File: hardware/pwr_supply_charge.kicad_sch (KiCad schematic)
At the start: 26 parts, among them J1 Battery Input, J2 Power Switch, J3 USB_C_Receptacle_USB2.0_14P, Q1 PSMN1R5-30YL, Q2 PSMN1R5-30YL, Q3 AO4435, Q4 AO4468, U1 HY2120, U2 CN3302

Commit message: updating component placcement
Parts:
- C1, C2: footprint Capacitor_SMD:C_0201_0603Metric -> Capacitor_SMD:C_0402_1005Metric
- R1, R2, R3: footprint Resistor_SMD:R_0603_1608Metric -> Resistor_SMD:R_0402_1005Metric
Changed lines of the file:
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@@
 			)
 		)
-		(property "Footprint" "Resistor_SMD:R_0603_1608Metric"
+		(property "Footprint" "Resistor_SMD:R_0402_1005Metric"
 			(at 168.91 33.528 90)
 			(effects
@@
 			)
 		)
-		(property "Footprint" "Resistor_SMD:R_0603_1608Metric"
+		(property "Footprint" "Resistor_SMD:R_0402_1005Metric"
 			(at 161.29 39.878 90)
 			(effects
@@
 			)
 		)
-		(property "Footprint" "Resistor_SMD:R_0603_1608Metric"
+		(property "Footprint" "Resistor_SMD:R_0402_1005Metric"
 			(at 214.122 50.8 90)
 			(effects
@@
 			)
 		)
-		(property "Footprint" "Capacitor_SMD:C_0201_0603Metric"
+		(property "Footprint" "Capacitor_SMD:C_0402_1005Metric"
 			(at 177.4952 44.45 0)
 			(effects
@@
 			)
 		)
-		(property "Footprint" "Capacitor_SMD:C_0201_0603Metric"
+		(property "Footprint" "Capacitor_SMD:C_0402_1005Metric"
 			(at 167.3352 46.99 0)
 			(effects

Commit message: Updating component placement
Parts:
- C3, C4: footprint Capacitor_SMD:C_0805_2012Metric -> Capacitor_SMD:CP_Elec_4x4.5
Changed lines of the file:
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@@
 			)
 		)
-		(property "Footprint" "Capacitor_SMD:C_0805_2012Metric"
+		(property "Footprint" "Capacitor_SMD:CP_Elec_4x4.5"
 			(at 228.2952 113.03 0)
 			(effects
@@
 			)
 		)
-		(property "Footprint" "Capacitor_SMD:C_0805_2012Metric"
+		(property "Footprint" "Capacitor_SMD:CP_Elec_4x4.5"
 			(at 117.8052 107.95 0)
 			(effects

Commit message: adding 3d models
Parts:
- J1: footprint Connector_JST:JST_XH_B3B-XH-AM_1x03_P2.50mm_Vertical -> Connector_JST:JST_XH_B3B-XH-A_1x03_P2.50mm_Vertical
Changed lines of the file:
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@@
 			)
 		)
-		(property "Footprint" "Connector_JST:JST_XH_B3B-XH-AM_1x03_P2.50mm_Vertical"
+		(property "Footprint" "Connector_JST:JST_XH_B3B-XH-A_1x03_P2.50mm_Vertical"
 			(at 93.98 38.1 0)
 			(effects

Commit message: adding inductor 3d model
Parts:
- L1: footprint Inductor_SMD:L_7.3x7.3_H3.5 -> Chromapi_FP:INDM6864X300N
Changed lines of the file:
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@@
 			)
 		)
-		(property "Footprint" "Inductor_SMD:L_7.3x7.3_H3.5"
+		(property "Footprint" "Chromapi_FP:INDM6864X300N"
 			(at 204.47 97.79 0)
 			(effects

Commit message: Updating schematic
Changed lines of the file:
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@@
 					(size 1.27 1.27)
 				)
+				(hide yes)
 			)
 		)
@@
 					(size 1.27 1.27)
 				)
+				(hide yes)
 			)
 		)
@@
 					(size 1.27 1.27)
 				)
+				(hide yes)
 			)
 		)
@@
 					(size 1.27 1.27)
 				)
+				(hide yes)
 			)
 		)
@@
 					(size 1.27 1.27)
 				)
-			)
-		)
+				(hide yes)
+			)
+		)

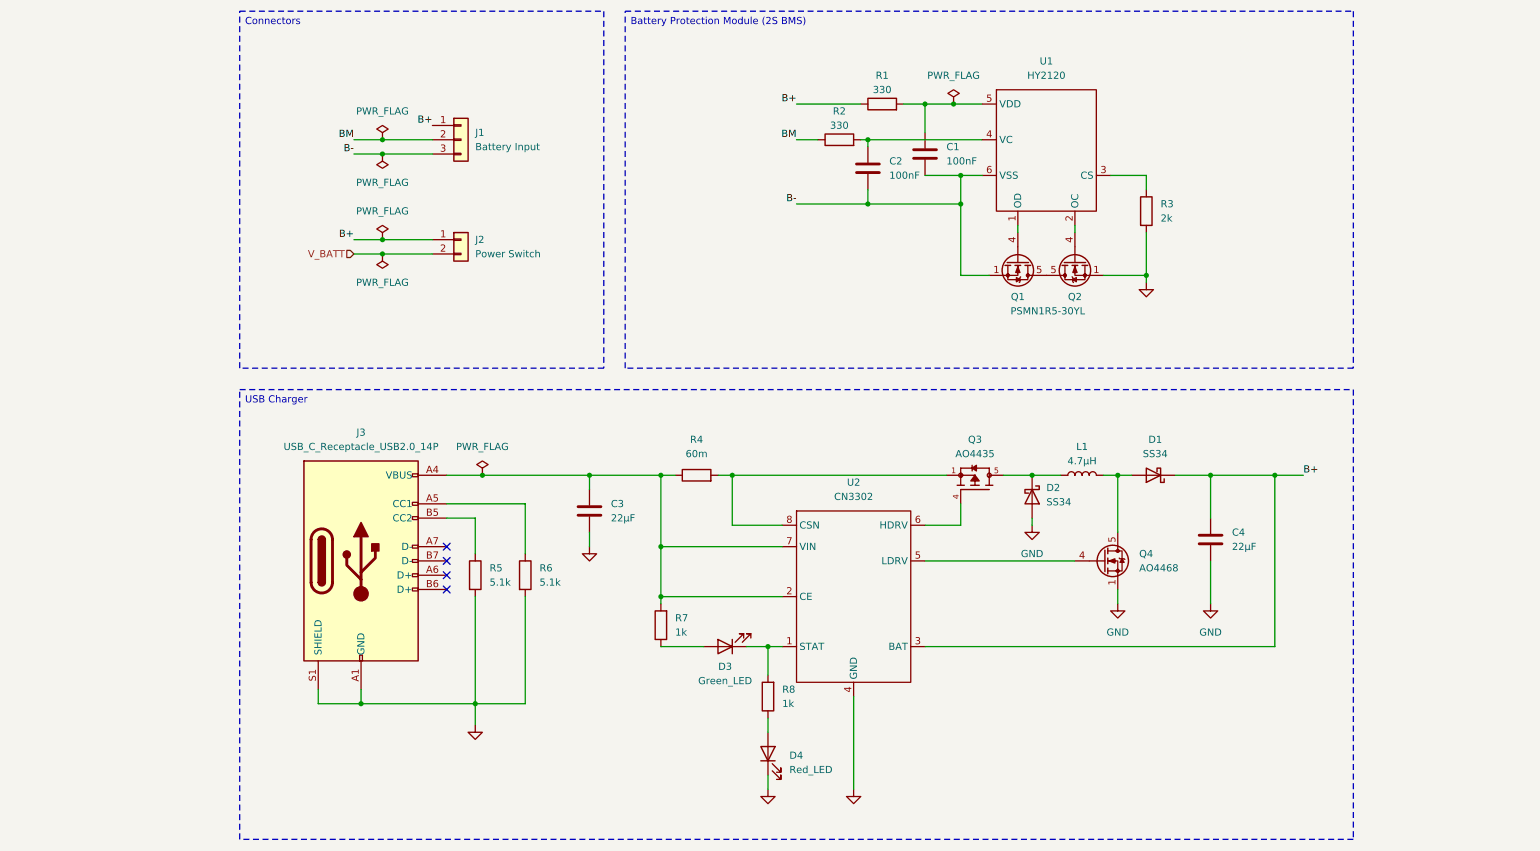
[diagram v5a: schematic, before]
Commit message: IMU modification and Power monitor addition
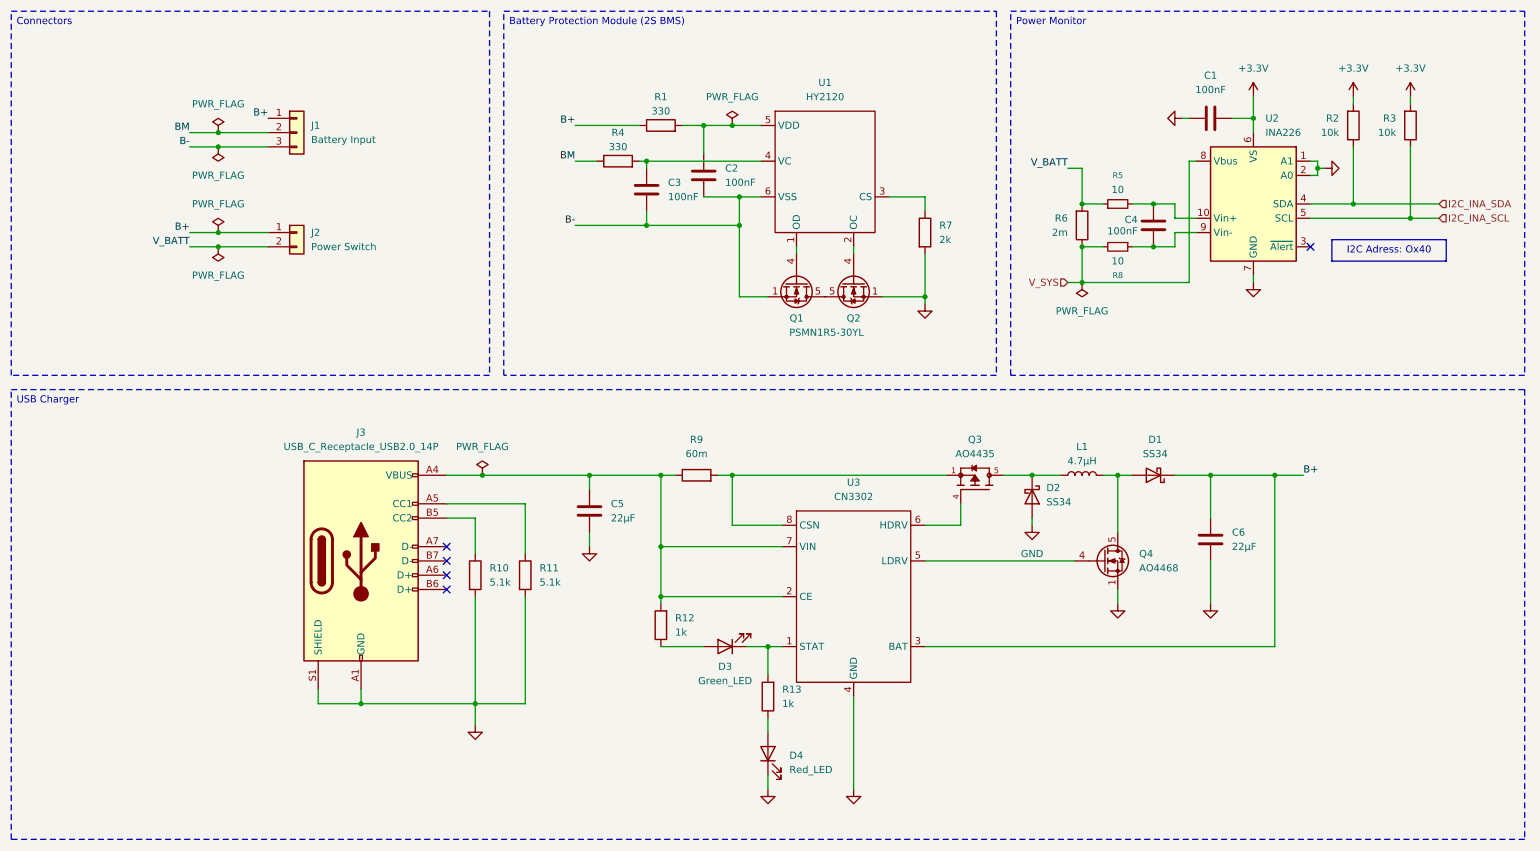
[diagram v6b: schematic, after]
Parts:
- added C1: 100nF, Capacitor_SMD:C_0603_1608Metric, symbol Device:C
- added C4: 100nF, Capacitor_SMD:CP_Elec_4x4.5, symbol Device:C
- added R2, R3: 10k, symbol Device:R
- added R5, R8: 10, symbol Device:R_Small
- added R6: 2m, symbol Device:R
- added U2: INA226, Package_SO:VSSOP-10_3x3mm_P0.5mm, symbol Sensor_Energy:INA226
- Q3: Availability In Stock -> (none); Description_1 P-Channel 30 V 10.5A (Ta) 3.1W (Ta) Surface Mount 8-SOIC -> (none); MANUFACTURER ALPHA & OMEGA SEMICONDUCTOR -> (none); MF Alpha & -> (none); MFN (none) -> Alpha & Omega Semiconductor; MP AO4435 -> (none); MPN (none) -> AO4435; Package SOIC-8 Alpha &amp; Omega Semiconductor -> SOIC-8 Alpha & Omega Semiconductor; Price None -> (none); SnapEDA_Link https://www.snapeda.com/parts/AO4435/Alpha/view-part/?ref=s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 -> (none)
- renumbered C1 to C2, C2 to C3, C3 to C5, C4 to C6, R5 to R10, R6 to R11, R7 to R12, R8 to R13, R2 to R4, R3 to R7, R4 to R9, U2 to U3
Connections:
- net GND: now also C1.2, U2.1 (A1), U2.2 (A0), U2.7 (GND)
- net V_BATT: now also R5.1, R6.2
- new net: C4.2, R8.1, U2.9 (Vin-)
- new net: C4.1, R5.2, U2.10 (Vin+)
- new net +3.3V: C1.1, R2.2, R3.2, U2.6 (VS)
- new net I2C_INA_SCL: R3.1, U2.5 (SCL)
- new net I2C_INA_SDA: R2.1, U2.4 (SDA)
- new net V_SYS: R6.1, R8.2, U2.8 (Vbus)
- no-connect marks 4 -> 5
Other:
- moved on the sheet: C2, C3, J1, J2, Q1, Q2, R1, R4, R7, U1

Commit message: Updating placement
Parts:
- C4: footprint Capacitor_SMD:CP_Elec_4x4.5 -> Capacitor_SMD:C_0603_1608Metric
- R2, R3: footprint (none) -> Resistor_SMD:R_0402_1005Metric
- R5, R8: footprint (none) -> Resistor_SMD:R_0603_1608Metric
- R6: footprint (none) -> Resistor_SMD:R_2512_6332Metric

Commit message: Replacing MOSFET for CSD17581Q3A
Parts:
- removed Q1, Q2: PSMN1R5-30YL, Package_TO_SOT_SMD:LFPAK56, symbol Transistor_FET:PSMN5R2-60YL
- added Q1, Q2: CSD17581Q3A, Package_SON:VSON-8_3.3x3.3mm_P0.65mm_NexFET, symbol Transistor_FET:CSD17581Q3A
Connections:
- net B-: now also Q1.1 (S), Q1.2 (S), Q1.3 (S)
- net GND: now also Q2.1 (S), Q2.2 (S), Q2.3 (S)
- net at U1.1 (OD): now also Q1.4 (G)
- net at U1.2 (OC): now also Q2.4 (G)
- net I2C_INA_SCL renamed INA226_SCL
- net I2C_INA_SDA renamed INA226_SDA
- new net: Q1.5 (D), Q2.5 (D)
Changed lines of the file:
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@@
 		)
 	)
-	(hierarchical_label "I2C_INA_SCL"
+	(hierarchical_label "INA226_SCL"
 		(shape input)
 		(at 267.97 52.07 0)
@@
 		)
 	)
-	(hierarchical_label "I2C_INA_SDA"
+	(hierarchical_label "INA226_SDA"
 		(shape input)
 		(at 267.97 49.53 0)
@@
 	)
 	(symbol
-		(lib_id "Transistor_FET:PSMN5R2-60YL")
-		(at 163.83 63.5 90)
-		(mirror x)
-		(unit 1)
-		(exclude_from_sim no)
-		(in_bom yes)
-		(on_board yes)
-		(dnp no)
-		(property "Reference" "Q2"
-			(at 163.83 69.85 90)
-			(effects
-				(font
-					(size 1.27 1.27)
-				)
-			)
-		)
-		(property "Value" "PSMN1R5-30YL"
-			(at 163.83 74.93 90)
-			(effects
-				(font
-					(size 1.27 1.27)
-				)
-				(hide yes)
-			)
-		)
-		(property "Footprint" "Package_TO_SOT_SMD:LFPAK56"
-			(at 165.735 68.58 0)
-			(effects
-				(font
-					(size 1.27 1.27)
-					(italic yes)
-				)
-				(justify left)
-				(hide yes)
-			)
-		)
-		(property "Datasheet" "https://github.com/Mowibox/chromapi_motherboard/blob/main/docs/datasheets/PSMN1R5-30YLC.pdf"
-			(at 167.64 68.58 0)
-			(effects
-				(font
-					(size 1.27 1.27)
-				)
-				(justify left)
-				(hide yes)
-			)
-		)
-		(property "Description" "100A, 30V Vds, N-Channel MOSFET, 1.55mOhm Ron, LFPAK56"
-			(at 163.83 63.5 0)
-			(effects
-				(font
-					(size 1.27 1.27)
-				)
-				(hide yes)
-			)
-		)
-		(property "Author" ""
-			(at 163.83 63.5 90)
-			(effects
-				(font
-					(size 1.27 1.27)
-				)
-				(hide yes)
-			)
-		)
-		(property "License" ""
-			(at 163.83 63.5 90)
-			(effects
-				(font
-					(size 1.27 1.27)
-				)
-				(hide yes)
-			)
-		)
-		(property "Manufacturer" ""
-			(at 163.83 63.5 90)
-			(effects
-				(font
-					(size 1.27 1.27)
-				)
-				(hide yes)
-			)
-		)
-		(pin "3"
-		)
-		(pin "2"
-		)
-		(pin "5"
-		)
-		(pin "4"
-		)
-		(pin "1"
-		)
-		(instances
-			(project "chromapi_motherboard_v1"
-				(path "/d1a31f26-03e0-43e1-89c1-031fe31befc5/2dc5047f-e6b9-4c1e-8ac3-300835122eb4"
-					(reference "Q2")
-					(unit 1)
-				)
-			)
-		)
-	)
-	(symbol
 		(lib_id "Device:C")
 		(at 227.33 109.22 0)
@@
 	)
 	(symbol
+		(lib_id "Transistor_FET:CSD17581Q3A")
+		(at 163.83 63.5 90)
+		(mirror x)
+		(unit 1)
+		(exclude_from_sim no)
+		(in_bom yes)
+		(on_board yes)
+		(dnp no)
+		(property "Reference" "Q2"
+			(at 163.83 69.85 90)
+			(effects
+				(font
+					(size 1.27 1.27)
+				)
+			)
+		)
+		(property "Value" "CSD17581Q3A"
+			(at 163.83 72.39 90)
+			(effects
+				(font
+					(size 1.27 1.27)
+				)
+				(hide yes)
+			)
+		)
+		(property "Footprint" "Package_SON:VSON-8_3.3x3.3mm_P0.65mm_NexFET"
+			(at 165.735 68.58 0)
+			(effects
+				(font
+					(size 1.27 1.27)
+					(italic yes)
+				)
+				(justify left)
+				(hide yes)
+			)
+		)
+		(property "Datasheet" "https://github.com/Mowibox/chromapi_motherboard/blob/main/docs/datasheets/csd17581q3a.pdf"
+			(at 167.64 68.58 0)
+			(effects
+				(font
+					(size 1.27 1.27)
+				)
+				(justify left)
+				(hide yes)
+			)
+		)
+		(property "Description" "60A Id, 30V Vds, NexFET N-Channel Power MOSFET, 3.2mOhm Ron, Qg Typ 20nC, VSON-8 3.3x3.3mm"
+			(at 163.83 63.5 0)
+			(effects
+				(font
+					(size 1.27 1.27)
+				)
+				(hide yes)
+			)
+		)
+		(pin "4"
+		)
+		(pin "2"
+		)
+		(pin "1"
+		)
+		(pin "5"
+		)
+		(pin "3"
+		)
+		(instances
+			(project "chromapi_motherboard_v1"
+				(path "/d1a31f26-03e0-43e1-89c1-031fe31befc5/2dc5047f-e6b9-4c1e-8ac3-300835122eb4"
+					(reference "Q2")
+					(unit 1)
+				)
+			)
+		)
+	)
+	(symbol
 		(lib_id "Device:R")
 		(at 262.89 35.56 0)
@@
 	)
 	(symbol
+		(lib_id "Transistor_FET:CSD17581Q3A")
+		(at 153.67 63.5 270)
+		(unit 1)
+		(exclude_from_sim no)
+		(in_bom yes)
+		(on_board yes)
+		(dnp no)
+		(property "Reference" "Q1"
+			(at 153.67 69.85 90)
+			(effects
+				(font
+					(size 1.27 1.27)
+				)
+			)
+		)
+		(property "Value" "CSD17581Q3A"
+			(at 158.75 72.644 90)
+			(effects
+				(font
+					(size 1.27 1.27)
+				)
+			)
+		)
+		(property "Footprint" "Package_SON:VSON-8_3.3x3.3mm_P0.65mm_NexFET"
+			(at 151.765 68.58 0)
+			(effects
+				(font
+					(size 1.27 1.27)
+					(italic yes)
+				)
+				(justify left)
+				(hide yes)
+			)
+		)
+		(property "Datasheet" "https://github.com/Mowibox/chromapi_motherboard/blob/main/docs/datasheets/csd17581q3a.pdf"
+			(at 149.86 68.58 0)
+			(effects
+				(font
+					(size 1.27 1.27)
+				)
+				(justify left)
+				(hide yes)
+			)
+		)
+		(property "Description" "60A Id, 30V Vds, NexFET N-Channel Power MOSFET, 3.2mOhm Ron, Qg Typ 20nC, VSON-8 3.3x3.3mm"
+			(at 153.67 63.5 0)
+			(effects
+				(font
+					(size 1.27 1.27)
+				)
+				(hide yes)
+			)
+		)
+		(pin "4"
+		)
+		(pin "2"
+		)
+		(pin "1"
+		)
+		(pin "5"
+		)
+		(pin "3"
+		)
+		(instances
+			(project ""
+				(path "/d1a31f26-03e0-43e1-89c1-031fe31befc5/2dc5047f-e6b9-4c1e-8ac3-300835122eb4"
+					(reference "Q1")
+					(unit 1)
+				)
+			)
+		)
+	)
+	(symbol
 		(lib_id "power:GND")
 		(at 176.53 67.31 0)
@@
 	)
 	(symbol
-		(lib_id "Transistor_FET:PSMN5R2-60YL")
-		(at 153.67 63.5 270)
-		(unit 1)
-		(exclude_from_sim no)
-		(in_bom yes)
-		(on_board yes)
-		(dnp no)
-		(property "Reference" "Q1"
-			(at 153.67 69.85 90)
-			(effects
-				(font
-					(size 1.27 1.27)
-				)
-			)
-		)
-		(property "Value" "PSMN1R5-30YL"
-			(at 159.004 72.39 90)
-			(effects
-				(font
-					(size 1.27 1.27)
-				)
-			)
-		)
-		(property "Footprint" "Package_TO_SOT_SMD:LFPAK56"
-			(at 151.765 68.58 0)
-			(effects
-				(font
-					(size 1.27 1.27)
-					(italic yes)
-				)
-				(justify left)
-				(hide yes)
-			)
-		)
-		(property "Datasheet" "https://github.com/Mowibox/chromapi_motherboard/blob/main/docs/datasheets/PSMN1R5-30YLC.pdf"
-			(at 149.86 68.58 0)
-			(effects
-				(font
-					(size 1.27 1.27)
-				)
-				(justify left)
-				(hide yes)
-			)
-		)
-		(property "Description" "100A, 30V Vds, N-Channel MOSFET, 1.55mOhm Ron, LFPAK56"
-			(at 153.67 63.5 0)
-			(effects
-				(font
-					(size 1.27 1.27)
-				)
-				(hide yes)
-			)
-		)
-		(property "Author" ""
-			(at 153.67 63.5 90)
-			(effects
-				(font
-					(size 1.27 1.27)
-				)
-				(hide yes)
-			)
-		)
-		(property "License" ""
-			(at 153.67 63.5 90)
-			(effects
-				(font
-					(size 1.27 1.27)
-				)
-				(hide yes)
-			)
-		)
-		(property "Manufacturer" ""
-			(at 153.67 63.5 90)
-			(effects
-				(font
-					(size 1.27 1.27)
-				)
-				(hide yes)
-			)
-		)
-		(pin "3"
-		)
-		(pin "2"
-		)
-		(pin "5"
-		)
-		(pin "4"
-		)
-		(pin "1"
-		)
-		(instances
-			(project ""
-				(path "/d1a31f26-03e0-43e1-89c1-031fe31befc5/2dc5047f-e6b9-4c1e-8ac3-300835122eb4"
-					(reference "Q1")
-					(unit 1)
-				)
-			)
-		)
-	)
-	(symbol
 		(lib_id "Device:R")
 		(at 204.47 53.34 0)
@@
 		(dnp no)
 		(fields_autoplaced yes)
-		(property "Reference" "#FLG07"
+		(property "Reference" "#FLG08"
 			(at 97.79 95.885 0)
 			(effects
@@
 			(project "chromapi_motherboard_v1"
 				(path "/d1a31f26-03e0-43e1-89c1-031fe31befc5/2dc5047f-e6b9-4c1e-8ac3-300835122eb4"
-					(reference "#FLG07")
+					(reference "#FLG08")
 					(unit 1)
 				)
@@
 		(dnp no)
 		(fields_autoplaced yes)
-		(property "Reference" "#FLG010"
+		(property "Reference" "#FLG07"
 			(at 204.47 65.405 0)
 			(effects
@@
 			(project "chromapi_motherboard_v1"
 				(path "/d1a31f26-03e0-43e1-89c1-031fe31befc5/2dc5047f-e6b9-4c1e-8ac3-300835122eb4"
-					(reference "#FLG010")
+					(reference "#FLG07")
 					(unit 1)
 				)
